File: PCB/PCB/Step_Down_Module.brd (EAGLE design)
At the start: 68 x 99.2 mm, 42 parts, among them Q1 TPH2900ENH

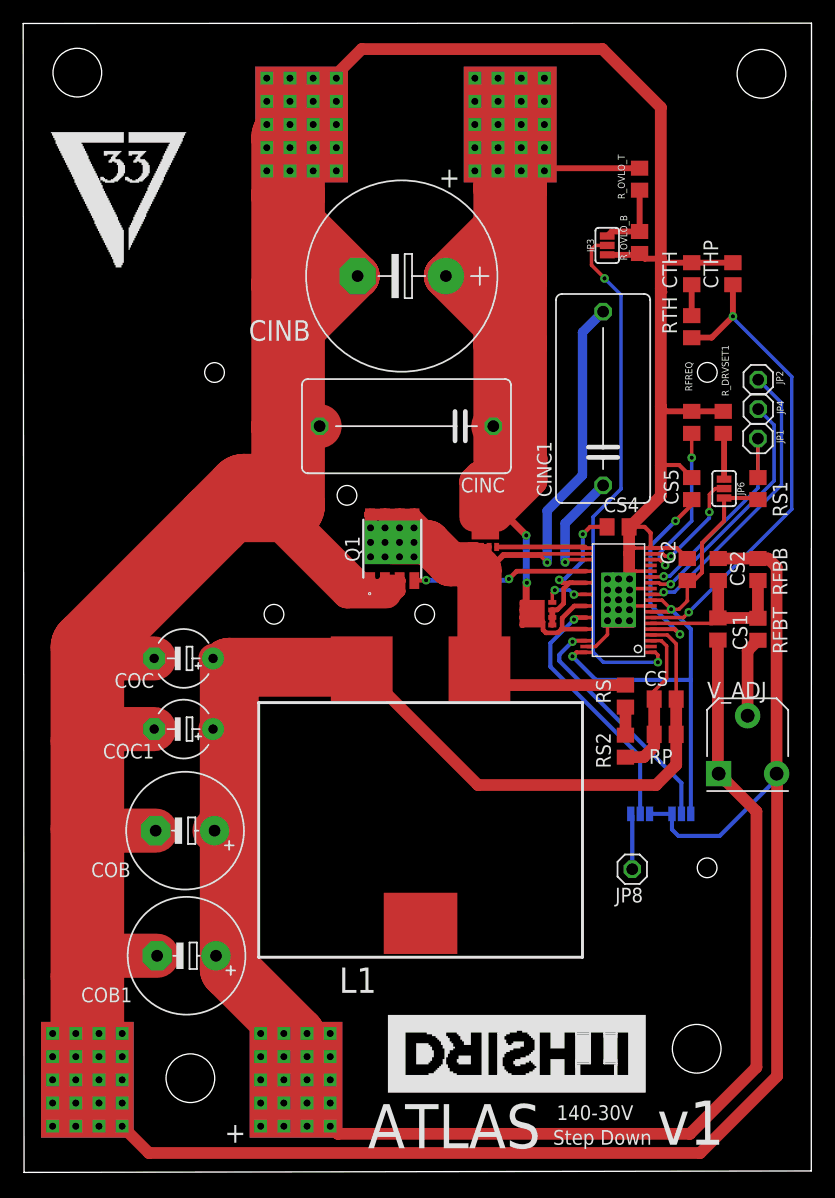
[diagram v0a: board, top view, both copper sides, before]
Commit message: PCB changes, added through hole part for RP, fixed pot error
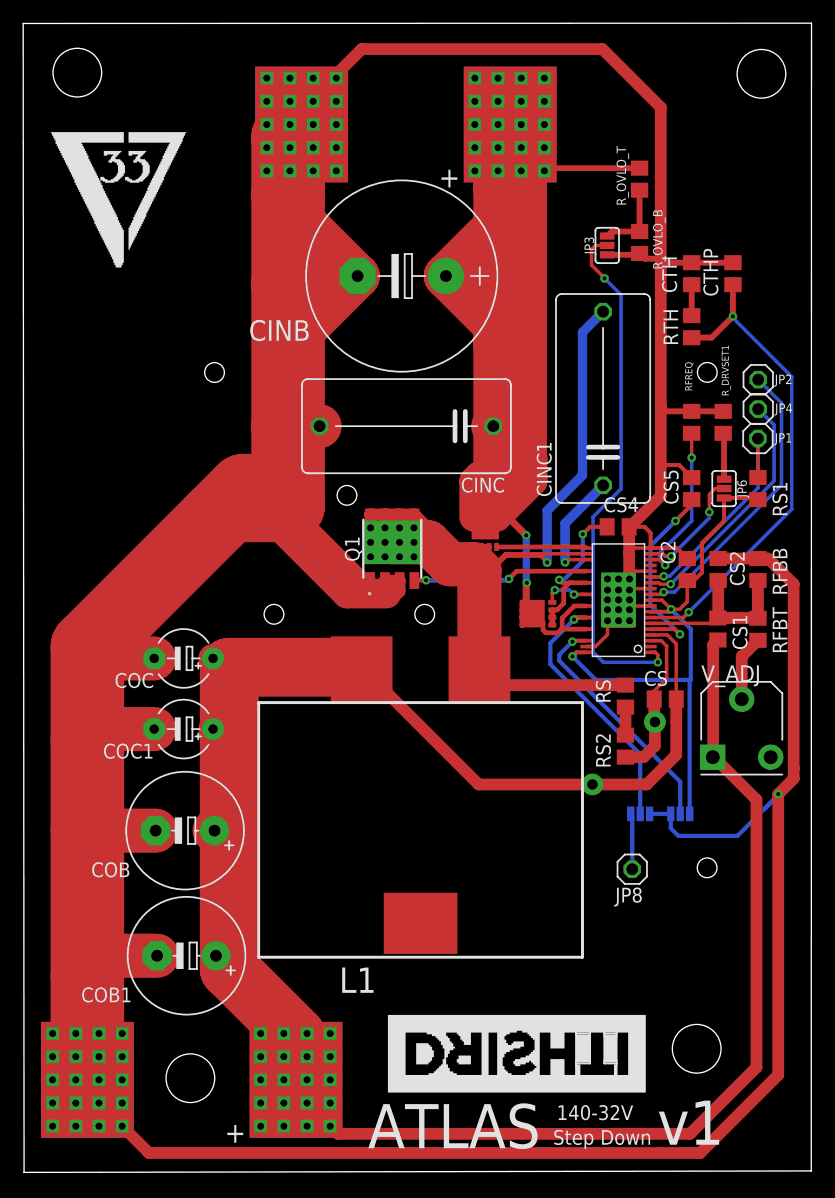
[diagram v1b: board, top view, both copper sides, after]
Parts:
- RP: device rcl:R0805 -> SparkFun-Resistors:AXIAL-0.3
- moved RP 3.93 mm to (51.8, 35.8), flipped to the bottom, turned to 315 degrees
- moved V_ADJ 1.51 mm to (62.0, 37.9)
- moved JP5 0.10 mm to (56.7, 30.5)
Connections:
- net GND: no longer V_ADJ.E
- net N$6: now also RP.P$1; no longer RP.2
- net VOUT: now also RP.P$2; no longer RP.1
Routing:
- net N$14: track 6.88 -> 5.66 mm
- net GND: track 604.0 -> 604.3 mm, vias 0 -> 1
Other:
- board text added: "140-32V"
- board text removed: "140-30V"
